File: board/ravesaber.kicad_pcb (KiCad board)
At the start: 2 copper layers, 24.6 x 108 mm, 22 parts, among them J1 BATT, J2 LED, J3 FTDI SERIAL, J4 ISP, J5 External Button, SW1 Button, SW2 Reset, U1 LM2576TV-5G, U2 ATmega168A-PU, Y1 16Mhz

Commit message: Fix Footprint Size for C2, Fix Silkscreen for L1
Create a new CP_Elec footprint using the datasheet for C2, swapping out
the footprint in the PCB schematic.

Fix the Silkscreen layer for the L1 footprint, ensuring it does not
cross the pads.

Shift the SW2 footprint up so that it's courtyard does not overlap the
courtyard of J4.
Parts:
- C2: footprint Capacitor_SMD:CP_Elec_16x17.5 -> Capacitor:CP_AFK158M16H32T
- moved SW2 0.11 mm to (111.0, 130.7)
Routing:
- net VCC: track 108.8 -> 101.5 mm
- net GND: track 105.5 -> 111.6 mm

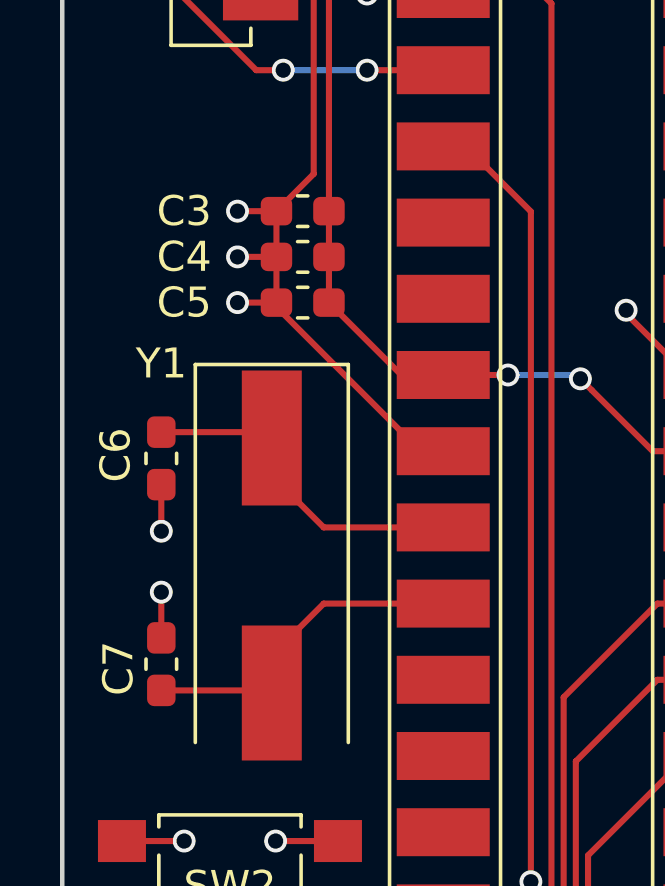
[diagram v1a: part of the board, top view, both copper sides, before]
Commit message: Change 0603 Capacitors to New Footprint
Switch the PCB footprints for the 0603 SMD Capacitors to the new
1.08x0.95mm hand-soldering version from KiCad 5.99.
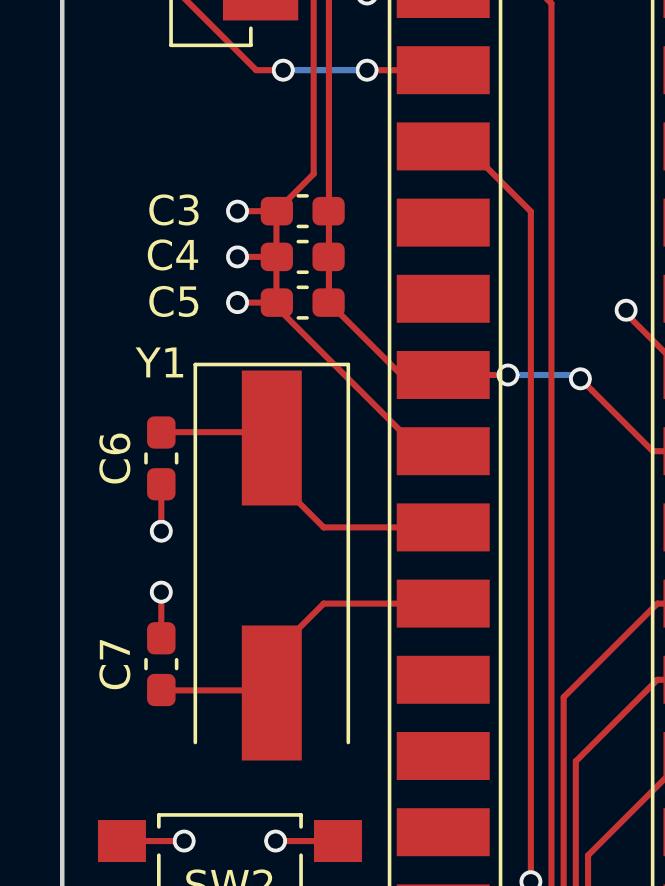
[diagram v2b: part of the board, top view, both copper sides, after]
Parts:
- C3, C4, C5, C6, C7: footprint Capacitor_SMD:C_0603_1608Metric_Pad1.05x0.95mm_HandSolder -> Capacitor_SMD:C_0603_1608Metric_Pad1.08x0.95mm_HandSolder
